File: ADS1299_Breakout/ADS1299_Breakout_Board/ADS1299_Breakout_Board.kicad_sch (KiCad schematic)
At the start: 38 parts, among them J1 Conn_01x08_Pin, J2 Conn_01x08_Pin, J3 Conn_01x08_Pin, J4 Conn_01x08_Pin, J5 Conn_01x08_Pin, U1 TPD4E1B06DRLR, U2 ADS1299IPAG, U3 TPD4E1B06DRLR, U4 TPD4E1B06DRLR, U5 TPD4E1B06DRLR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

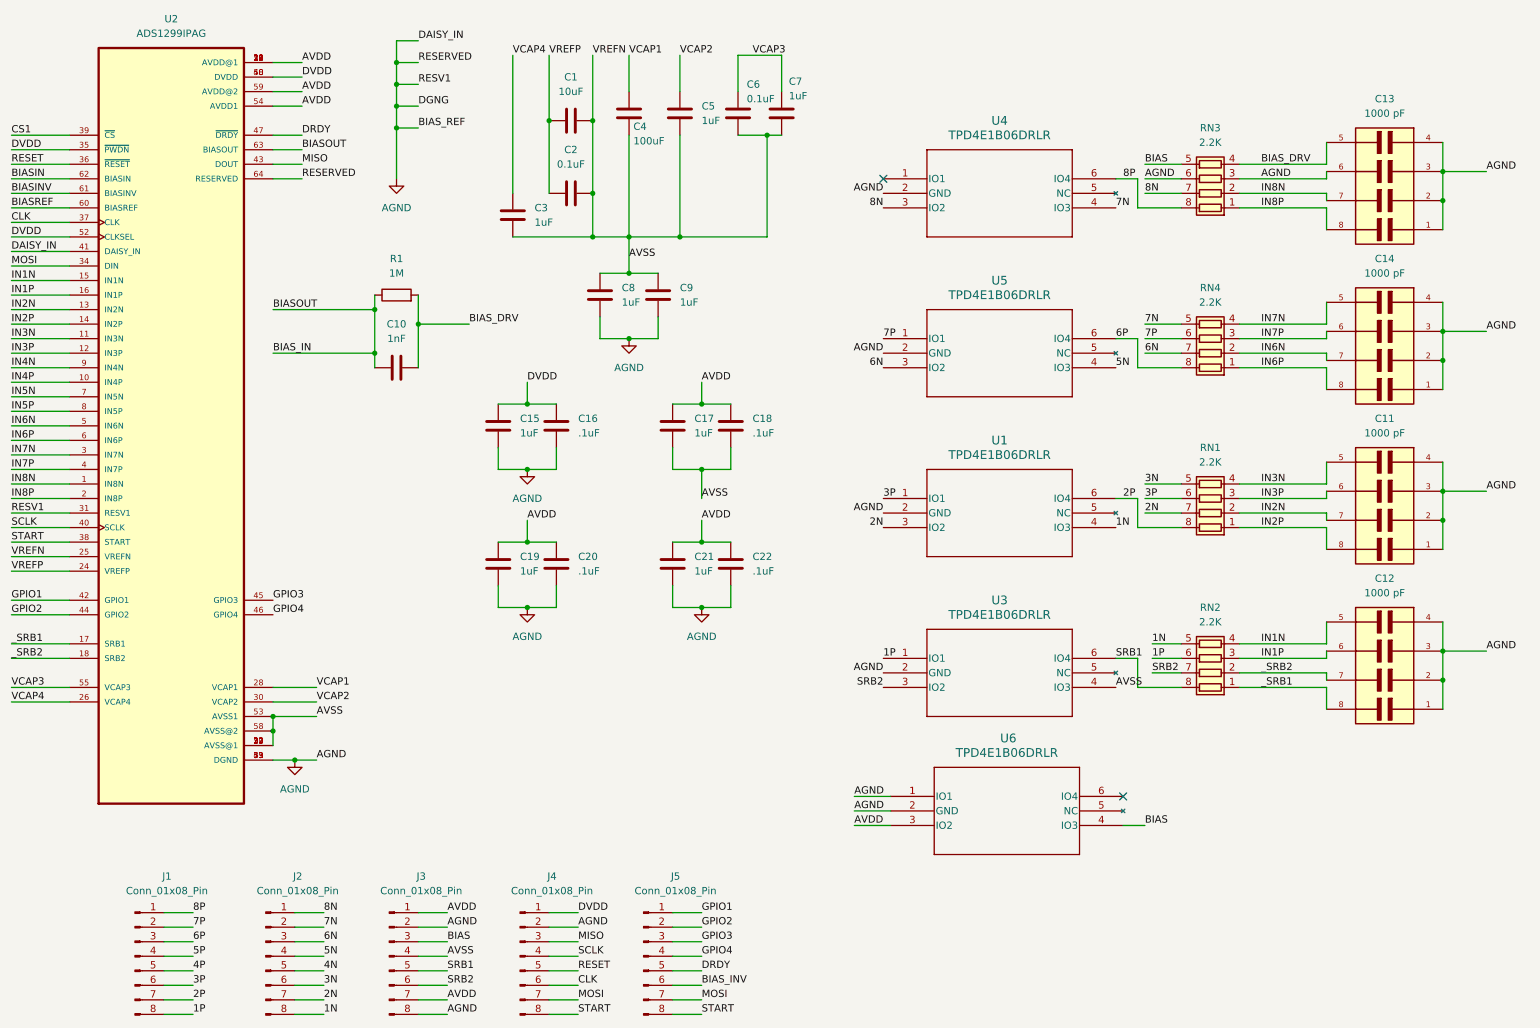
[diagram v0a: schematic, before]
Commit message: Fixed some of the label names and started work on pcb
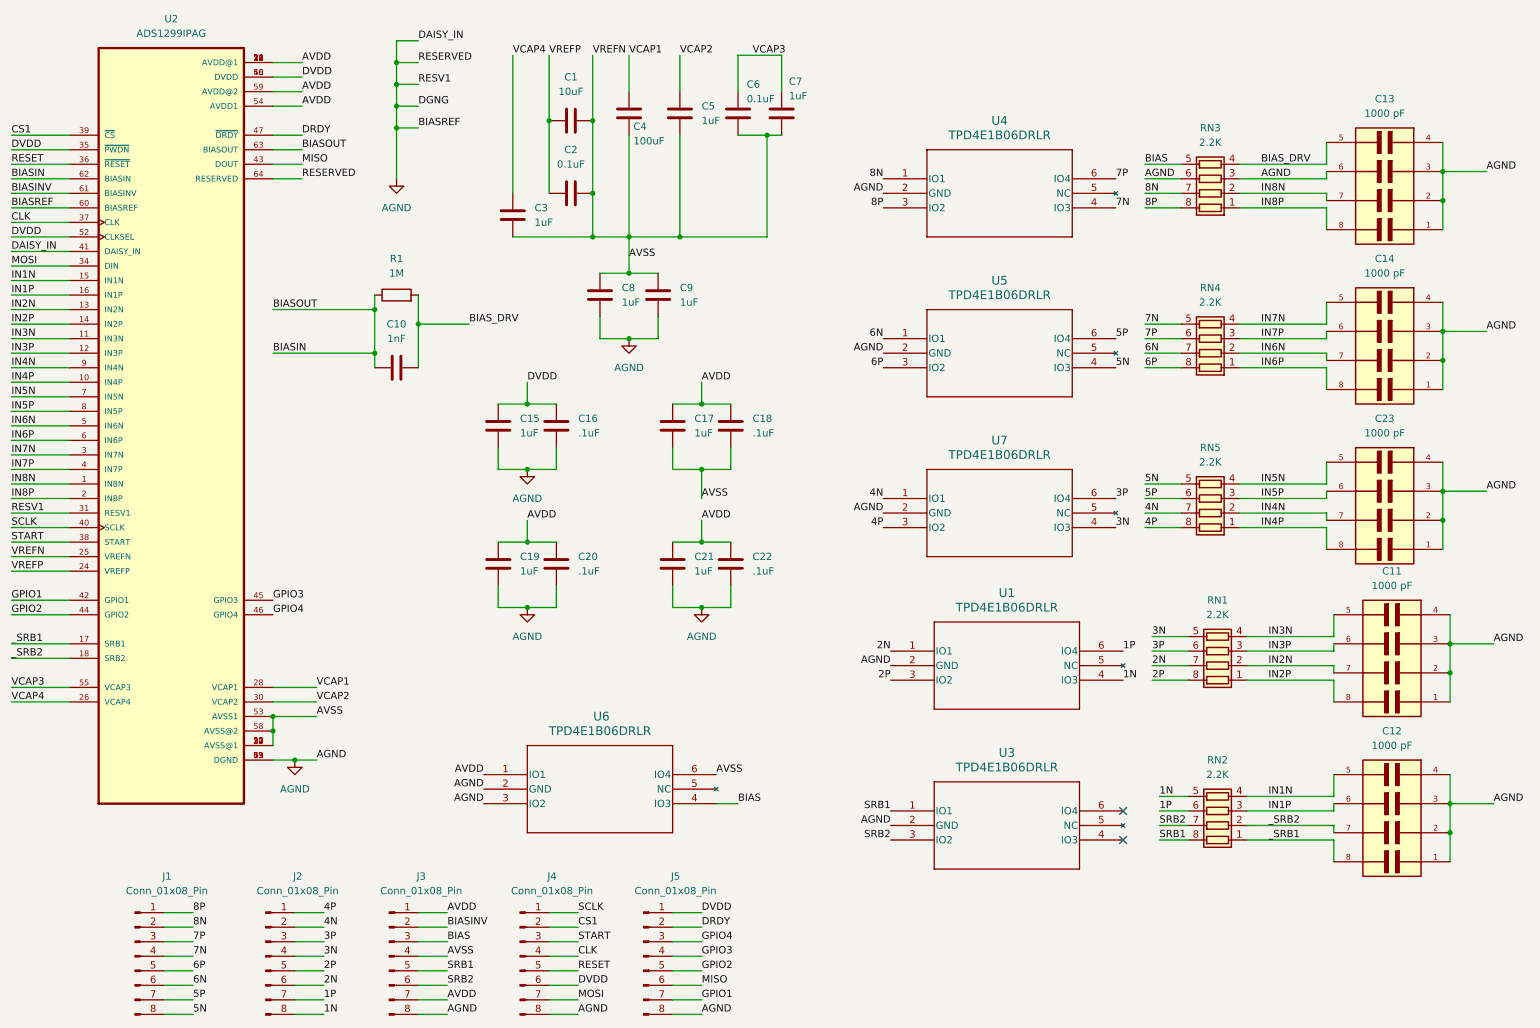
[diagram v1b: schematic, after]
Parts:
- added C23: 1000 pF, CAPCAF50P200X125X85-8, symbol W3A45C102K4T2A (C_array):CKCL44X7R1H102M085AA
- added RN5: 2.2K, Resistor_SMD:R_Array_Concave_4x0603, symbol Device:R_Pack04
- added U7: TPD4E1B06DRLR, DRL6_TEX, symbol TPD4E1B06 (ESD):TPD4E1B06DRLR
- C11, C12, C13, C14: footprint CKCL44X7R1H102M085AA:CAPCAF50P200X125X85-8 -> CAPCAF50P200X125X85-8
- J1, J2, J3, J4, J5: footprint (none) -> Connector_PinHeader_2.54mm:PinHeader_1x08_P2.54mm_Vertical
- U2: footprint ADS1299IPAG:QFP50P1200X1200X120-64N -> QFP50P1200X1200X120-64N
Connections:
- net BIASOUT is gone; now on net BIASIN: C10.2, R1.1, U2.63 (BIASOUT)
- net BIASREF is gone; now on net AGND: U2.60 (BIASREF)
- net BIAS_INV is gone; now on net MISO: J5.6 (Pin_6)
- net 1P: now also J2.7 (Pin_7), U1.6 (IO4); no longer J1.8 (Pin_8), U3.1 (IO1)
- net 2N: now also J2.6 (Pin_6), U1.1 (IO1); no longer J2.7 (Pin_7), U1.3 (IO2)
- net 2P: now also J2.5 (Pin_5), U1.3 (IO2); no longer J1.7 (Pin_7), U1.6 (IO4)
- net 3N: now also J2.4 (Pin_4), U7.4 (IO3); no longer J2.6 (Pin_6)
- net 3P: now also J2.3 (Pin_3), U7.6 (IO4); no longer J1.6 (Pin_6), U1.1 (IO1)
- net 4N: now also J2.2 (Pin_2), RN5.7 (R2.2), U7.1 (IO1); no longer J2.5 (Pin_5)
- net 4P: now also J2.1 (Pin_1), RN5.8 (R1.2), U7.3 (IO2); no longer J1.5 (Pin_5)
- net 5N: now also J1.8 (Pin_8), RN5.5 (R4.2); no longer J2.4 (Pin_4)
- net 5P: now also J1.7 (Pin_7), U5.6 (IO4), RN5.6 (R3.2); no longer J1.4 (Pin_4)
- net 6N: now also J1.6 (Pin_6), U5.1 (IO1); no longer J2.3 (Pin_3), U5.3 (IO2)
- net 6P: now also J1.5 (Pin_5), U5.3 (IO2); no longer J1.3 (Pin_3), U5.6 (IO4)
- net 7N: now also J1.4 (Pin_4); no longer J2.2 (Pin_2)
- net 7P: now also J1.3 (Pin_3), U4.6 (IO4); no longer J1.2 (Pin_2), U5.1 (IO1)
- net 8N: now also J1.2 (Pin_2), U4.1 (IO1); no longer J2.1 (Pin_1), U4.3 (IO2)
- net 8P: now also U4.3 (IO2); no longer U4.6 (IO4)
- net AGND: now also J4.8 (Pin_8), J5.8 (Pin_8), U6.3 (IO2), C23.1, C23.2, C23.3, C23.4, U7.2 (GND); no longer J3.2 (Pin_2), J4.2 (Pin_2), U6.1 (IO1)
- net AVDD: now also U6.1 (IO1); no longer U6.3 (IO2)
- net AVSS: now also U6.6 (IO4); no longer U3.4 (IO3)
- net BIASINV: now also J3.2 (Pin_2)
- net CLK: now also J4.4 (Pin_4); no longer J4.6 (Pin_6)
- net CS1: now also J4.2 (Pin_2)
- net DRDY: now also J5.2 (Pin_2); no longer J5.5 (Pin_5)
- net DVDD: now also J4.6 (Pin_6), J5.1 (Pin_1); no longer J4.1 (Pin_1)
- net GPIO1: now also J5.7 (Pin_7); no longer J5.1 (Pin_1)
- net GPIO2: now also J5.5 (Pin_5); no longer J5.2 (Pin_2)
- net GPIO3: now also J5.4 (Pin_4); no longer J5.3 (Pin_3)
- net GPIO4: now also J5.3 (Pin_3); no longer J5.4 (Pin_4)
- net IN4N: now also C23.7, RN5.2 (R2.1)
- net IN4P: now also C23.8, RN5.1 (R1.1)
- net IN5N: now also C23.5, RN5.4 (R4.1)
- net IN5P: now also C23.6, RN5.3 (R3.1)
- net MISO: no longer J4.3 (Pin_3)
- net MOSI: no longer J5.7 (Pin_7)
- net SCLK: now also J4.1 (Pin_1); no longer J4.4 (Pin_4)
- net SRB1: now also U3.1 (IO1); no longer U3.6 (IO4)
- net START: now also J4.3 (Pin_3); no longer J4.8 (Pin_8), J5.8 (Pin_8)
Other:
- moved on the sheet: C11, C12, RN1, RN2, U1, U3, U6

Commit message: Finished up traces
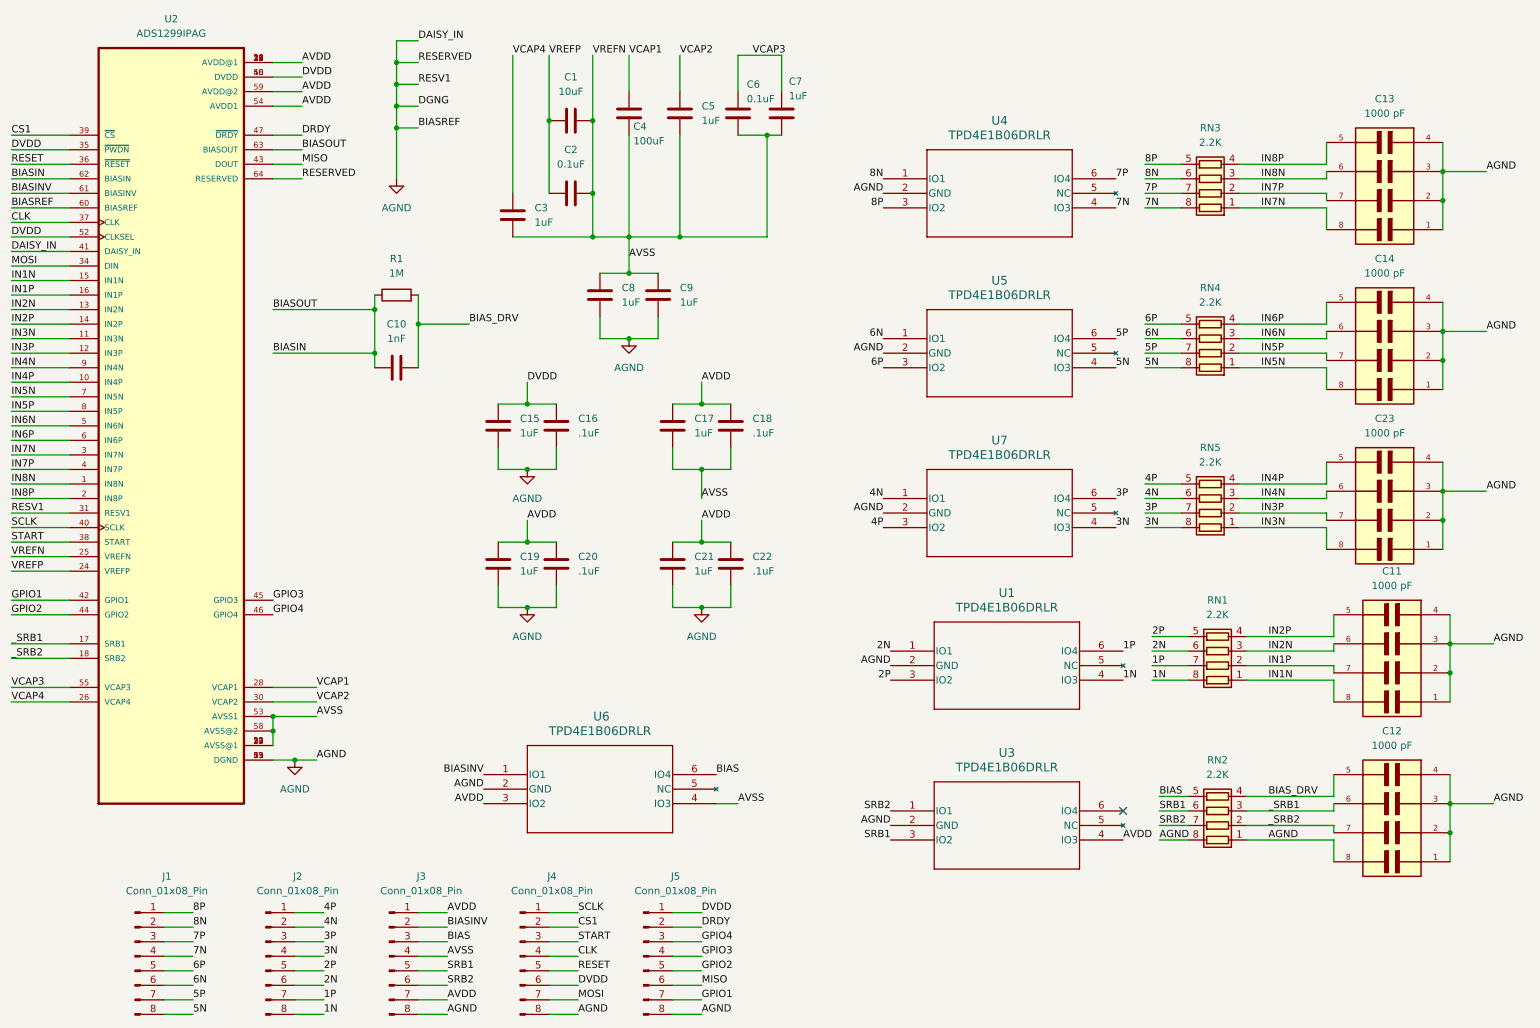
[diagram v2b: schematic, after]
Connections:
- net 1N: now also RN1.8 (R1.2); no longer RN2.5 (R4.2)
- net 1P: now also RN1.7 (R2.2); no longer RN2.6 (R3.2)
- net 2N: now also RN1.6 (R3.2); no longer RN1.7 (R2.2)
- net 2P: now also RN1.5 (R4.2); no longer RN1.8 (R1.2)
- net 3N: now also RN5.8 (R1.2); no longer RN1.5 (R4.2)
- net 3P: now also RN5.7 (R2.2); no longer RN1.6 (R3.2)
- net 4N: now also RN5.6 (R3.2); no longer RN5.7 (R2.2)
- net 4P: now also RN5.5 (R4.2); no longer RN5.8 (R1.2)
- net 5N: now also RN4.8 (R1.2); no longer RN5.5 (R4.2)
- net 5P: now also RN4.7 (R2.2); no longer RN5.6 (R3.2)
- net 6N: now also RN4.6 (R3.2); no longer RN4.7 (R2.2)
- net 6P: now also RN4.5 (R4.2); no longer RN4.8 (R1.2)
- net 7N: now also RN3.8 (R1.2); no longer RN4.5 (R4.2)
- net 7P: now also RN3.7 (R2.2); no longer RN4.6 (R3.2)
- net 8N: now also RN3.6 (R3.2); no longer RN3.7 (R2.2)
- net 8P: now also RN3.5 (R4.2); no longer RN3.8 (R1.2)
- net AGND: now also C12.8, RN2.1 (R1.1), RN2.8 (R1.2); no longer C13.6, RN3.3 (R3.1), RN3.6 (R3.2), U6.3 (IO2)
- net AVDD: now also U3.4 (IO3), U6.3 (IO2); no longer U6.1 (IO1)
- net AVSS: now also U6.4 (IO3); no longer U6.6 (IO4)
- net BIAS: now also RN2.5 (R4.2), U6.6 (IO4); no longer RN3.5 (R4.2), U6.4 (IO3)
- net BIASINV: now also U6.1 (IO1)
- net BIAS_DRV: now also C12.5, RN2.4 (R4.1); no longer C13.5, RN3.4 (R4.1)
- net IN1N: now also C11.8, RN1.1 (R1.1); no longer C12.5, RN2.4 (R4.1)
- net IN1P: now also C11.7, RN1.2 (R2.1); no longer C12.6, RN2.3 (R3.1)
- net IN2N: now also C11.6, RN1.3 (R3.1); no longer C11.7, RN1.2 (R2.1)
- net IN2P: now also C11.5, RN1.4 (R4.1); no longer C11.8, RN1.1 (R1.1)
- net IN3N: now also C23.8, RN5.1 (R1.1); no longer C11.5, RN1.4 (R4.1)
- net IN3P: now also C23.7, RN5.2 (R2.1); no longer C11.6, RN1.3 (R3.1)
- net IN4N: now also C23.6, RN5.3 (R3.1); no longer C23.7, RN5.2 (R2.1)
- net IN4P: now also C23.5, RN5.4 (R4.1); no longer C23.8, RN5.1 (R1.1)
- net IN5N: now also C14.8, RN4.1 (R1.1); no longer C23.5, RN5.4 (R4.1)
- net IN5P: now also C14.7, RN4.2 (R2.1); no longer C23.6, RN5.3 (R3.1)
- net IN6N: now also C14.6, RN4.3 (R3.1); no longer C14.7, RN4.2 (R2.1)
- net IN6P: now also C14.5, RN4.4 (R4.1); no longer C14.8, RN4.1 (R1.1)
- net IN7N: now also C13.8, RN3.1 (R1.1); no longer C14.5, RN4.4 (R4.1)
- net IN7P: now also C13.7, RN3.2 (R2.1); no longer C14.6, RN4.3 (R3.1)
- net IN8N: now also C13.6, RN3.3 (R3.1); no longer C13.7, RN3.2 (R2.1)
- net IN8P: now also C13.5, RN3.4 (R4.1); no longer C13.8, RN3.1 (R1.1)
- net SRB1: now also RN2.6 (R3.2), U3.3 (IO2); no longer RN2.8 (R1.2), U3.1 (IO1)
- net SRB2: now also U3.1 (IO1); no longer U3.3 (IO2)
- net _SRB1: now also C12.6, RN2.3 (R3.1); no longer C12.8, RN2.1 (R1.1)
- no-connect marks 2 -> 1
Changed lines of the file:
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@@
 	)
 	(no_connect
-		(at 212.09 157.48)
-	)
-	(no_connect
 		(at 212.09 152.4)
 	)
@@
 		)
 	)
-	(label "3P"
+	(label "2N"
 		(at 217.17 124.46 0)
 		(fields_autoplaced yes)
@@
 		)
 	)
-	(label "6P"
+	(label "5N"
 		(at 215.9 74.93 0)
 		(fields_autoplaced yes)
@@
 		)
 	)
-	(label "5N"
+	(label "4P"
 		(at 215.9 95.25 0)
 		(fields_autoplaced yes)
@@
 		)
 	)
-	(label "7N"
+	(label "SRB2"
+		(at 171.45 152.4 180)
+		(fields_autoplaced yes)
+		(effects
+			(font
+				(size 1.27 1.27)
+			)
+			(justify right bottom)
+		)
+	)
+	(label "6P"
 		(at 215.9 67.31 0)
 		(fields_autoplaced yes)
@@
 		)
 	)
-	(label "_SRB1"
+	(label "AGND"
 		(at 237.49 157.48 0)
 		(fields_autoplaced yes)
@@
 		)
 	)
-	(label "1P"
+	(label "SRB1"
 		(at 218.44 152.4 0)
 		(fields_autoplaced yes)
@@
 		)
 	)
+	(label "SRB1"
+		(at 171.45 157.48 180)
+		(fields_autoplaced yes)
+		(effects
+			(font
+				(size 1.27 1.27)
+			)
+			(justify right bottom)
+		)
+	)
 	(label "AVDD"
 		(at 68.58 21.59 0)
@@
 		)
 	)
-	(label "BIAS"
+	(label "8P"
 		(at 215.9 39.37 0)
 		(fields_autoplaced yes)
@@
 		)
 	)
-	(label "IN2N"
+	(label "IN1P"
 		(at 237.49 127 0)
 		(fields_autoplaced yes)
@@
 		)
 	)
-	(label "7P"
+	(label "6N"
 		(at 215.9 69.85 0)
 		(fields_autoplaced yes)
@@
 		)
 	)
-	(label "AGND"
+	(label "IN8N"
 		(at 236.22 41.91 0)
 		(fields_autoplaced yes)
@@
 		)
 	)
-	(label "AGND"
+	(label "8N"
 		(at 215.9 41.91 0)
 		(fields_autoplaced yes)
@@
 		)
 	)
-	(label "3N"
+	(label "2P"
 		(at 217.17 121.92 0)
 		(fields_autoplaced yes)
@@
 		)
 	)
-	(label "IN6P"
+	(label "IN5N"
 		(at 236.22 74.93 0)
 		(fields_autoplaced yes)
@@
 		)
 	)
-	(label "AVSS"
+	(label "BIAS"
 		(at 140.97 146.05 0)
 		(fields_autoplaced yes)
@@
 		)
 	)
-	(label "IN7P"
+	(label "IN6N"
 		(at 236.22 69.85 0)
 		(fields_autoplaced yes)
@@
 		)
 	)
-	(label "IN1N"
+	(label "BIAS_DRV"
 		(at 237.49 149.86 0)
 		(fields_autoplaced yes)
@@
 		)
 	)
-	(label "IN8P"
+	(label "IN7N"
 		(at 236.22 46.99 0)
 		(fields_autoplaced yes)
@@
 		)
 	)
-	(label "IN1P"
+	(label "_SRB1"
 		(at 237.49 152.4 0)
 		(fields_autoplaced yes)
@@
 		)
 	)
-	(label "IN3N"
+	(label "IN2P"
 		(at 237.49 121.92 0)
 		(fields_autoplaced yes)
@@
 		)
 	)
-	(label "IN3P"
+	(label "IN2N"
 		(at 237.49 124.46 0)
 		(fields_autoplaced yes)
@@
 		)
 	)
-	(label "2N"
+	(label "1P"
 		(at 217.17 127 0)
 		(fields_autoplaced yes)
@@
 		)
 	)
-	(label "4P"
+	(label "3N"
 		(at 215.9 102.87 0)
 		(fields_autoplaced yes)
@@
 		)
 	)
-	(label "AGND"
+	(label "AVDD"
 		(at 100.33 151.13 180)
 		(fields_autoplaced yes)
@@
 		)
 	)
-	(label "BIAS"
+	(label "AVSS"
 		(at 144.78 151.13 0)
 		(fields_autoplaced yes)
@@
 		)
 	)
-	(label "IN4N"
+	(label "IN3P"
 		(at 236.22 100.33 0)
 		(fields_autoplaced yes)
@@
 		)
 	)
-	(label "4N"
+	(label "3P"
 		(at 215.9 100.33 0)
 		(fields_autoplaced yes)
@@
 		)
 	)
-	(label "IN8N"
+	(label "IN7P"
 		(at 236.22 44.45 0)
 		(fields_autoplaced yes)
@@
 		)
 	)
-	(label "IN5P"
+	(label "IN4N"
 		(at 236.22 97.79 0)
 		(fields_autoplaced yes)
@@
 		)
 	)
-	(label "AVDD"
+	(label "BIASINV"
 		(at 100.33 146.05 180)
 		(fields_autoplaced yes)
@@
 		)
 	)
-	(label "5P"
+	(label "4N"
 		(at 215.9 97.79 0)
 		(fields_autoplaced yes)
@@
 		)
 	)
-	(label "IN7N"
+	(label "IN6P"
 		(at 236.22 67.31 0)
 		(fields_autoplaced yes)
@@
 		)
 	)
-	(label "IN4P"
+	(label "IN3N"
 		(at 236.22 102.87 0)
 		(fields_autoplaced yes)
@@
 		)
 	)
-	(label "SRB2"
-		(at 171.45 157.48 180)
-		(fields_autoplaced yes)
-		(effects
-			(font
-				(size 1.27 1.27)
-			)
-			(justify right bottom)
-		)
-	)
 	(label "AGND"
 		(at 275.59 40.64 0)
@@
 		)
 	)
-	(label "6N"
+	(label "5P"
 		(at 215.9 72.39 0)
 		(fields_autoplaced yes)
@@
 		)
 	)
-	(label "8N"
+	(label "7P"
 		(at 215.9 44.45 0)
 		(fields_autoplaced yes)
@@
 		)
 	)
-	(label "2P"
+	(label "1N"
 		(at 217.17 129.54 0)
 		(fields_autoplaced yes)
@@
 		)
 	)
-	(label "IN2P"
+	(label "IN1N"
 		(at 237.49 129.54 0)
 		(fields_autoplaced yes)
@@
 		)
 	)
-	(label "8P"
+	(label "AVDD"
+		(at 212.09 157.48 0)
+		(fields_autoplaced yes)
+		(effects
+			(font
+				(size 1.27 1.27)
+			)
+			(justify left bottom)
+		)
+	)
+	(label "7N"
 		(at 215.9 46.99 0)
 		(fields_autoplaced yes)
@@
 		)
 	)
-	(label "SRB1"
+	(label "AGND"
 		(at 218.44 157.48 0)
 		(fields_autoplaced yes)
@@
 		)
 	)
-	(label "BIAS_DRV"
+	(label "IN8P"
 		(at 236.22 39.37 0)
 		(fields_autoplaced yes)
@@
 		)
 	)
-	(label "SRB1"
-		(at 171.45 152.4 180)
-		(fields_autoplaced yes)
-		(effects
-			(font
-				(size 1.27 1.27)
-			)
-			(justify right bottom)
-		)
-	)
-	(label "1N"
+	(label "BIAS"
 		(at 218.44 149.86 0)
 		(fields_autoplaced yes)
@@
 		)
 	)
-	(label "IN5N"
+	(label "IN4P"
 		(at 236.22 95.25 0)
 		(fields_autoplaced yes)
@@
 		)
 	)
-	(label "IN6N"
+	(label "IN5P"
 		(at 236.22 72.39 0)
 		(fields_autoplaced yes)
